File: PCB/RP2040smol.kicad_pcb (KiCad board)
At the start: 4 copper layers, 25 x 25 mm, 40 parts, among them SW1 BOOTSEL, SW2 RESET, U1 AP2112K-3.3, U2 RP2040, U3 W25Q64JVZP, Y1 Crystal_520-120-18-33JGN-TR3

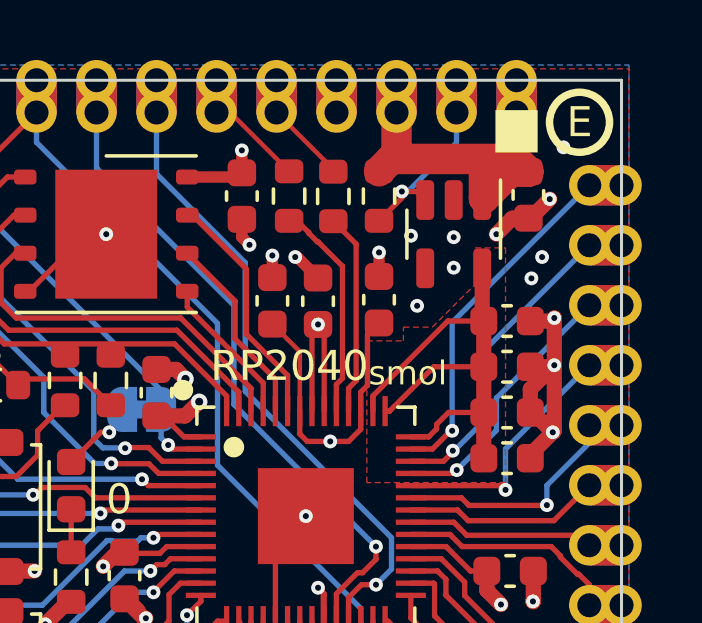
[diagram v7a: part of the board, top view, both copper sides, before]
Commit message: 3v3 vias
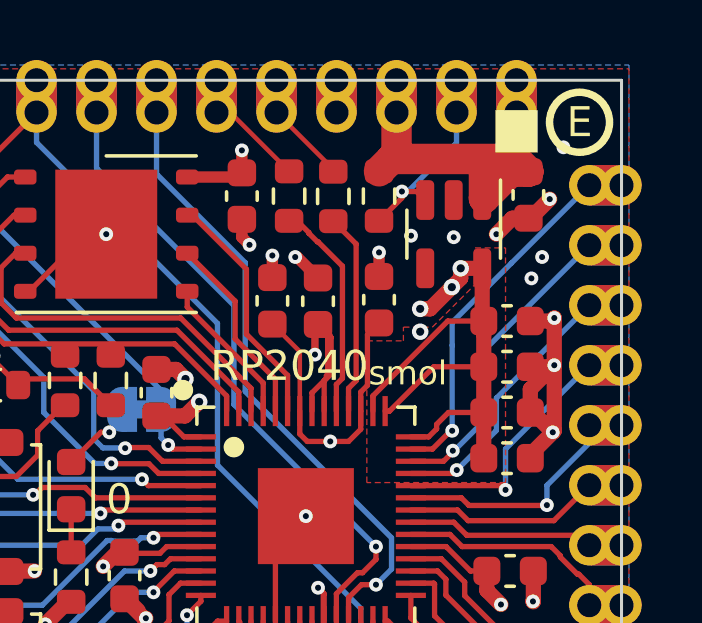
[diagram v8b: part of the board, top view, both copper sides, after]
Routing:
- net +3V3: track 47.3 -> 52.0 mm, vias 8 -> 12
- net GND: vias 35 -> 33
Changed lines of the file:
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@@
   (via (at 144.4832 101.6816) (size 0.46) (drill 0.2) (layers "F.Cu" "B.Cu") (free) (net 2))
   (via (at 141.0796 119.4108) (size 0.46) (drill 0.2) (layers "F.Cu" "B.Cu") (net 2))
-  (via (at 145.9056 102.7484) (size 0.46) (drill 0.2) (layers "F.Cu" "B.Cu") (free) (net 2))
   (via (at 147.7852 116.2612) (size 0.46) (drill 0.2) (layers "F.Cu" "B.Cu") (net 2))
   (via (at 132.2912 114.6356) (size 0.46) (drill 0.2) (layers "F.Cu" "B.Cu") (net 2))
@@
   (via (at 131.9356 112.8576) (size 0.46) (drill 0.2) (layers "F.Cu" "B.Cu") (net 2))
   (via (at 140.6224 102.3928) (size 0.46) (drill 0.2) (layers "F.Cu" "B.Cu") (net 2))
-  (via (at 144.6864 104.0184) (size 0.46) (drill 0.2) (layers "F.Cu" "B.Cu") (free) (net 2))
   (via (at 139.0984 101.9864) (size 0.46) (drill 0.2) (layers "F.Cu" "B.Cu") (net 2))
   (via (at 139.8604 102.342) (size 0.46) (drill 0.2) (layers "F.Cu" "B.Cu") (net 2))
@@
   (segment (start 136.336745 112.0448) (end 136.112734 112.268811) (width 0.1778) (layer "F.Cu") (net 3))
   (segment (start 147.0102 112.8576) (end 147.0102 113.505) (width 0.508) (layer "F.Cu") (net 3))
+  (segment (start 141.74 104.9966) (end 141.74 106.310202) (width 0.25) (layer "F.Cu") (net 3))
   (segment (start 134.9328 112.235) (end 134.6918 112.235) (width 0.508) (layer "F.Cu") (net 3))
   (segment (start 130.521216 105.686784) (end 130.521216 105.792216) (width 0.1778) (layer "F.Cu") (net 3))
   (segment (start 146.4644 112.8576) (end 147.0102 112.8576) (width 0.1778) (layer "F.Cu") (net 3))
+  (segment (start 146.8556 102.7683) (end 146.8556 102.8144) (width 0.508) (layer "F.Cu") (net 3))
   (segment (start 141.1812 114.5288) (end 141.1812 116.1466) (width 0.1778) (layer "F.Cu") (net 3))
-  (segment (start 146.9086 104.5264) (end 146.9086 106.0504) (width 0.508) (layer "F.Cu") (net 3))
-  (segment (start 141.1812 107.5288) (end 141.1812 104.8442) (width 0.1778) (layer "F.Cu") (net 3))
+  (segment (start 146.9086 104.5264) (end 146.9086 104.9706) (width 0.508) (layer "F.Cu") (net 3))
   (segment (start 145.336389 107.969266) (end 145.731255 107.5744) (width 0.1778) (layer "F.Cu") (net 3))
   (segment (start 144.478001 108.3872) (end 145.069537 108.3872) (width 0.1778) (layer "F.Cu") (net 3))
+  (segment (start 141.3844 104.641) (end 141.74 104.9966) (width 0.25) (layer "F.Cu") (net 3))
+  (segment (start 141.717627 106.383627) (end 141.1812 106.920054) (width 0.1778) (layer "F.Cu") (net 3))
   (segment (start 136.9518 107.689) (end 137.422 107.2188) (width 0.508) (layer "F.Cu") (net 3))
+  (segment (start 146.1397 103.100206) (end 145.842953 103.396953) (width 0.508) (layer "F.Cu") (net 3))
   (segment (start 138.8444 99.5858) (end 138.8444 98.8876) (width 0.381) (layer "F.Cu") (net 3))
   (segment (start 134.6918 112.235) (end 134.2216 112.7052) (width 0.508) (layer "F.Cu") (net 3))
+  (segment (start 141.81988 105.07648) (end 141.5876 104.8442) (width 0.1778) (layer "F.Cu") (net 3))
   (segment (start 131.5922 106.4568) (end 133.5998 106.4568) (width 0.1778) (layer "F.Cu") (net 3))
+  (segment (start 146.9086 104.9706) (end 146.9086 106.0504) (width 0.508) (layer "F.Cu") (net 3))
   (segment (start 137.478 112.0448) (end 136.336745 112.0448) (width 0.1778) (layer "F.Cu") (net 3))
   (segment (start 145.6516 112.0448) (end 146.4644 112.8576) (width 0.1778) (layer "F.Cu") (net 3))
+  (segment (start 141.5876 106.513654) (end 141.717627 106.383627) (width 0.1778) (layer "F.Cu") (net 3))
   (segment (start 145.2452 106.0504) (end 146.9086 106.0504) (width 0.1778) (layer "F.Cu") (net 3))
   (segment (start 145.7093 104.5264) (end 146.9086 104.5264) (width 0.1778) (layer "F.Cu") (net 3))
+  (segment (start 141.81988 106.281374) (end 141.81988 105.07648) (width 0.1778) (layer "F.Cu") (net 3))
   (segment (start 146.8556 102.7683) (end 146.8556 104.4734) (width 0.508) (layer "F.Cu") (net 3))
+  (segment (start 145.842953 103.396953) (end 145.119906 104.12) (width 0.508) (layer "F.Cu") (net 3))
   (segment (start 144.478 112.0448) (end 145.6516 112.0448) (width 0.1778) (layer "F.Cu") (net 3))
   (segment (start 147.0102 113.505) (end 147.4804 113.9752) (width 0.508) (layer "F.Cu") (net 3))
   (segment (start 135.9996 107.689) (end 136.9518 107.689) (width 0.508) (layer "F.Cu") (net 3))
+  (segment (start 141.717627 106.383627) (end 141.81988 106.281374) (width 0.1778) (layer "F.Cu") (net 3))
   (segment (start 130.521216 105.792216) (end 131.389 106.66) (width 0.1778) (layer "F.Cu") (net 3))
+  (segment (start 146.1397 102.7683) (end 146.1397 103.100206) (width 0.508) (layer "F.Cu") (net 3))
   (segment (start 146.9086 106.0504) (end 146.9086 107.5744) (width 0.508) (layer "F.Cu") (net 3))
+  (segment (start 145.119906 104.12) (end 144.788 104.12) (width 0.508) (layer "F.Cu") (net 3))
+  (segment (start 141.1812 106.920054) (end 141.1812 107.5288) (width 0.1778) (layer "F.Cu") (net 3))
   (segment (start 136.2158 107.689) (end 136.914 108.3872) (width 0.1778) (layer "F.Cu") (net 3))
+  (segment (start 141.2805 105.644) (end 141.2805 104.7449) (width 0.25) (layer "F.Cu") (net 3))
   (segment (start 133.5998 106.4568) (end 134.4756 107.3326) (width 0.1778) (layer "F.Cu") (net 3))
   (segment (start 143.6196 107.528799) (end 143.766801 107.528799) (width 0.1778) (layer "F.Cu") (net 3))
   (segment (start 136.112734 112.268811) (end 134.966611 112.268811) (width 0.1778) (layer "F.Cu") (net 3))
-  (segment (start 141.5876 107.5288) (end 141.5876 104.8442) (width 0.1778) (layer "F.Cu") (net 3))
   (segment (start 143.2132 107.0225) (end 145.7093 104.5264) (width 0.1778) (layer "F.Cu") (net 3))
   (segment (start 141.9432 116.9216) (end 141.3336 117.5312) (width 0.508) (layer "F.Cu") (net 3))
   (segment (start 145.731255 107.5744) (end 146.9086 107.5744) (width 0.1778) (layer "F.Cu") (net 3))
+  (segment (start 141.2805 104.7449) (end 141.3844 104.641) (width 0.25) (layer "F.Cu") (net 3))
   (segment (start 141.1812 116.1466) (end 141.9432 116.9086) (width 0.1778) (layer "F.Cu") (net 3))
+  (segment (start 141.74 106.310202) (end 141.692101 106.358101) (width 0.25) (layer "F.Cu") (net 3))
+  (segment (start 146.8556 102.7683) (end 146.1397 102.7683) (width 0.508) (layer "F.Cu") (net 3))
   (segment (start 145.069537 108.3872) (end 145.336389 108.120348) (width 0.1778) (layer "F.Cu") (net 3))
   (segment (start 136.914 108.3872) (end 137.478 108.3872) (width 0.1778) (layer "F.Cu") (net 3))
   (segment (start 137.0232 99.7258) (end 138.7044 99.7258) (width 0.381) (layer "F.Cu") (net 3))
+  (segment (start 141.5876 107.5288) (end 141.5876 106.513654) (width 0.1778) (layer "F.Cu") (net 3))
   (segment (start 138.8444 98.8876) (end 138.8444 98.8368) (width 0.381) (layer "F.Cu") (net 3))
   (segment (start 145.336389 108.120348) (end 145.336389 107.969266) (width 0.1778) (layer "F.Cu") (net 3))
+  (via (at 144.788 104.882) (size 0.55) (drill 0.27) (layers "F.Cu" "B.Cu") (free) (net 3))
+  (via (at 146.1397 102.7683) (size 0.55) (drill 0.27) (layers "F.Cu" "B.Cu") (net 3))
   (via (at 138.8444 98.8368) (size 0.46) (drill 0.2) (layers "F.Cu" "B.Cu") (net 3))
-  (via (at 141.3844 104.641) (size 0.46) (drill 0.2) (layers "F.Cu" "B.Cu") (net 3))
+  (via (at 141.2805 105.644) (size 0.46) (drill 0.2) (layers "F.Cu" "B.Cu") (net 3))
+  (via (at 144.788 104.12) (size 0.55) (drill 0.27) (layers "F.Cu" "B.Cu") (net 3))
   (via (at 147.4804 113.9752) (size 0.46) (drill 0.2) (layers "F.Cu" "B.Cu") (net 3))
   (via (at 130.521216 105.686784) (size 0.55) (drill 0.27) (layers "F.Cu" "B.Cu") (net 3))
+  (via (at 145.842953 103.396953) (size 0.55) (drill 0.27) (layers "F.Cu" "B.Cu") (net 3))
   (via (at 137.422 107.2188) (size 0.55) (drill 0.27) (layers "F.Cu" "B.Cu") (net 3))
   (via (at 148.86568 117.902273) (size 0.46) (drill 0.2) (layers "F.Cu" "B.Cu") (net 3))
@@
   (segment (start 145.806349 108.184) (end 145.196749 108.7936) (width 0.1778) (layer "F.Cu") (net 55))
   (via (at 145.8548 108.184) (size 0.46) (drill 0.2) (layers "F.Cu" "B.Cu") (net 55))
-  (segment (start 145.8548 104.5702) (end 150.425 100) (width 0.1778) (layer "B.Cu") (net 55))
-  (segment (start 145.8548 108.184) (end 145.8548 104.5702) (width 0.1778) (layer "B.Cu") (net 55))
+  (segment (start 145.8548 105.3392) (end 145.8548 104.5702) (width 0.1778) (layer "B.Cu") (net 55))
+  (segment (start 147.8325 102.5925) (end 150.425 100) (width 0.1778) (layer "B.Cu") (net 55))
+  (segment (start 145.8548 104.5702) (end 147.8325 102.5925) (width 0.1778) (layer "B.Cu") (net 55))
+  (segment (start 145.8548 108.184) (end 145.8548 105.3392) (width 0.1778) (layer "B.Cu") (net 55))
   (segment (start 146.414448 110.6732) (end 146.160448 110.4192) (width 0.1778) (layer "F.Cu") (net 56))
   (segment (start 149.001135 110.6732) (end 146.414448 110.6732) (width 0.1778) (layer "F.Cu") (net 56))
